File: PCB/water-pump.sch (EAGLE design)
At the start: 26 parts, among them U1 LDL1117S12R, U3 ATSAMD11C14A-SSUT

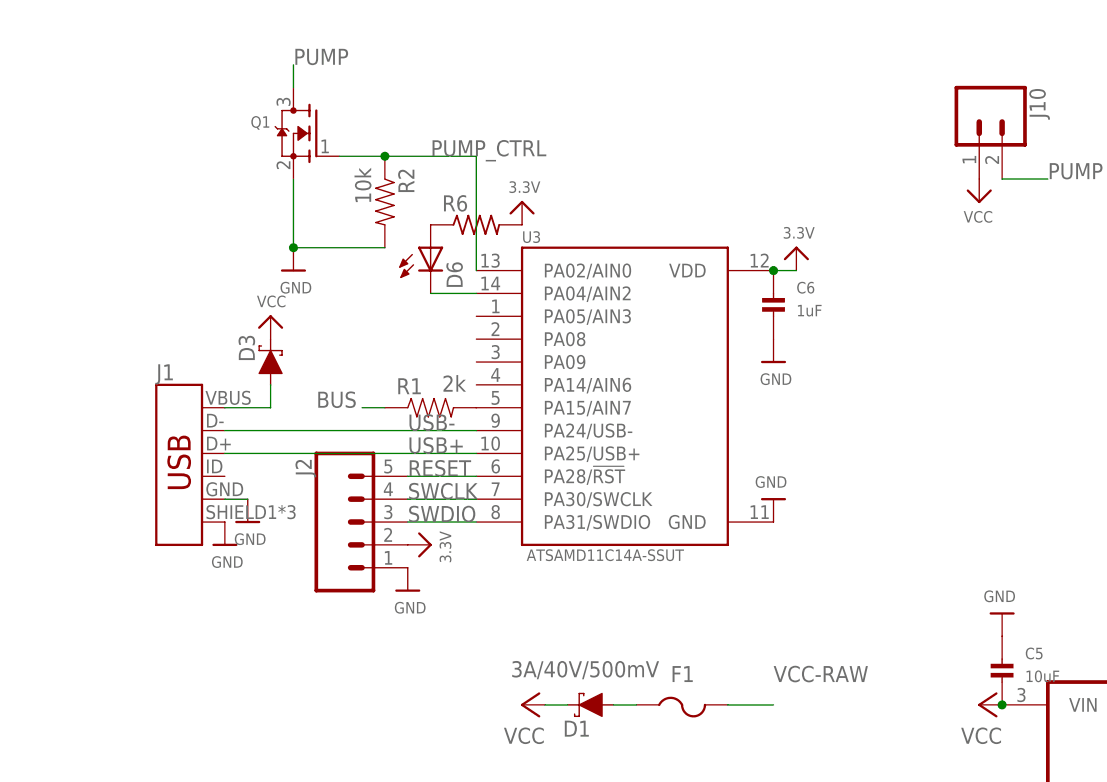
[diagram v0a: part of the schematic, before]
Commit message: added button to pcbs and did some fixing
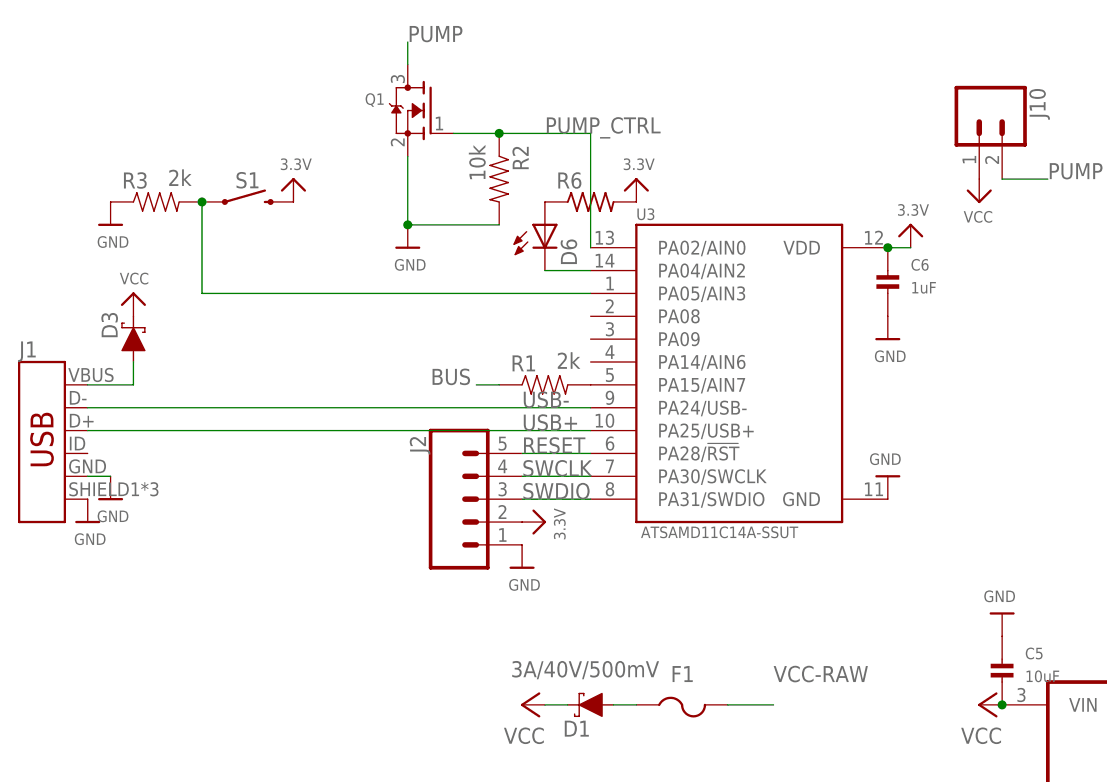
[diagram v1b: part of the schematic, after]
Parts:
- added R3: 2k, SparkFun-Resistors:RESISTOR1206
- added S1: MOMENTARY-SWITCH-SPST-SMD-6.0X3.5MM, SparkFun-Switches:MOMENTARY-SWITCH-SPST-SMD-6.0X3.5MM
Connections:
- new net N$4: R3.2, S1.1, U3.PA05/AIN3
- net 3.3V: now also S1.2
- net GND: now also R3.1
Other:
- moved on the sheet: C6, D3, D6, J1, J2, Q1, R1, R2, R6, U3

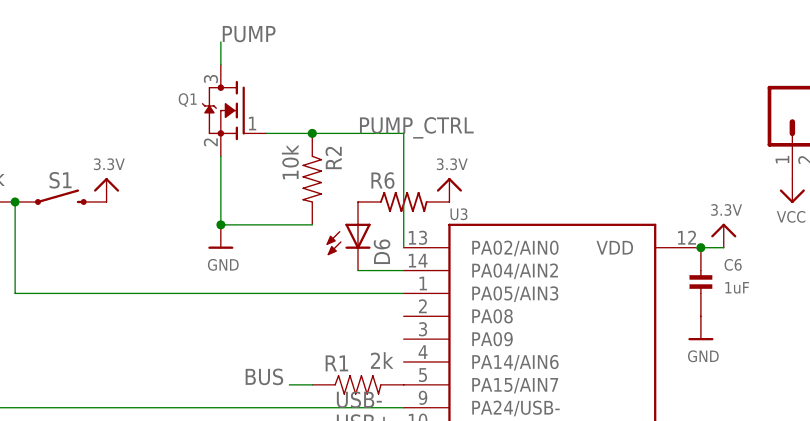
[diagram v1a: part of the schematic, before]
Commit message: added missing resistor before mosfet
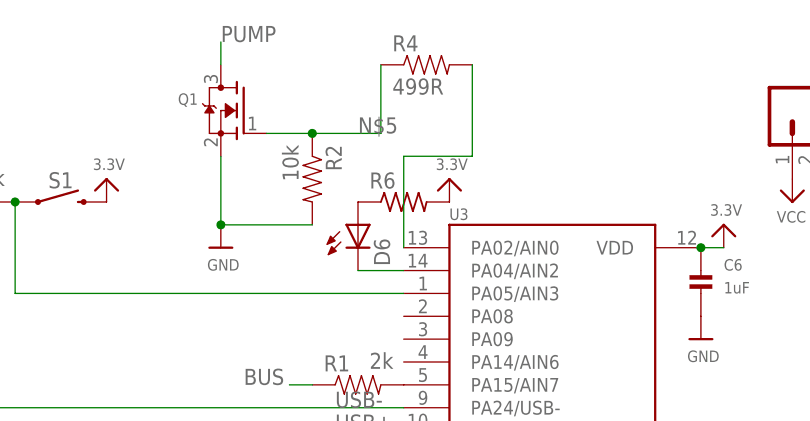
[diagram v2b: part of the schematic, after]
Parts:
- added R4: 499R, SparkFun-Resistors:RESISTOR1206
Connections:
- new net N$5: Q1.G, R2.1, R4.1
- net PUMP_CTRL: now also R4.2; no longer Q1.G, R2.1
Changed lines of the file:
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@@
 <?xml version="1.0" encoding="utf-8"?>
 <!DOCTYPE eagle SYSTEM "eagle.dtd">
-<eagle version="9.2.2">
+<eagle version="9.3.0">
 <drawing>
 <settings>
@@
 <part name="R3" library="SparkFun-Resistors" deviceset="RESISTOR" device="1206" value="2k"/>
 <part name="S1" library="SparkFun-Switches" deviceset="MOMENTARY-SWITCH-SPST" device="-SMD-6.0X3.5MM"/>
+<part name="R4" library="SparkFun-Resistors" deviceset="RESISTOR" device="1206" value="499R"/>
 </parts>
 <sheets>
@@
 <attribute name="NAME" x="-81.28" y="67.564" size="1.778" layer="95" font="vector" align="bottom-center"/>
 </instance>
+<instance part="R4" gate="G$1" x="-40.64" y="81.28" smashed="yes">
+<attribute name="NAME" x="-44.45" y="82.7786" size="1.778" layer="95"/>
+<attribute name="VALUE" x="-44.45" y="77.978" size="1.778" layer="96"/>
+</instance>
 </instances>
 <busses>
@@
 <net name="PUMP_CTRL" class="0">
 <segment>
-<pinref part="R2" gate="G$1" pin="1"/>
-<label x="-48.26" y="73.66" size="1.778" layer="95"/>
 <pinref part="U3" gate="G$1" pin="PA02/AIN0"/>
-<wire x1="-53.34" y1="73.66" x2="-43.18" y2="73.66" width="0.1524" layer="91"/>
-<wire x1="-43.18" y1="73.66" x2="-43.18" y2="60.96" width="0.1524" layer="91"/>
-<pinref part="Q1" gate="G$1" pin="G"/>
-<wire x1="-58.42" y1="73.66" x2="-53.34" y2="73.66" width="0.1524" layer="91"/>
-<junction x="-53.34" y="73.66"/>
+<wire x1="-43.18" y1="71.12" x2="-43.18" y2="60.96" width="0.1524" layer="91"/>
+<pinref part="R4" gate="G$1" pin="2"/>
+<wire x1="-43.18" y1="71.12" x2="-35.56" y2="71.12" width="0.1524" layer="91"/>
+<wire x1="-35.56" y1="71.12" x2="-35.56" y2="81.28" width="0.1524" layer="91"/>
 </segment>
 </net>
@@
 </segment>
 </net>
+<net name="N$5" class="0">
+<segment>
+<pinref part="R4" gate="G$1" pin="1"/>
+<wire x1="-45.72" y1="73.66" x2="-45.72" y2="81.28" width="0.1524" layer="91"/>
+<pinref part="R2" gate="G$1" pin="1"/>
+<wire x1="-53.34" y1="73.66" x2="-45.72" y2="73.66" width="0.1524" layer="91"/>
+<junction x="-53.34" y="73.66"/>
+<pinref part="Q1" gate="G$1" pin="G"/>
+<wire x1="-58.42" y1="73.66" x2="-53.34" y2="73.66" width="0.1524" layer="91"/>
+<label x="-48.26" y="73.66" size="1.778" layer="95"/>
+</segment>
+</net>

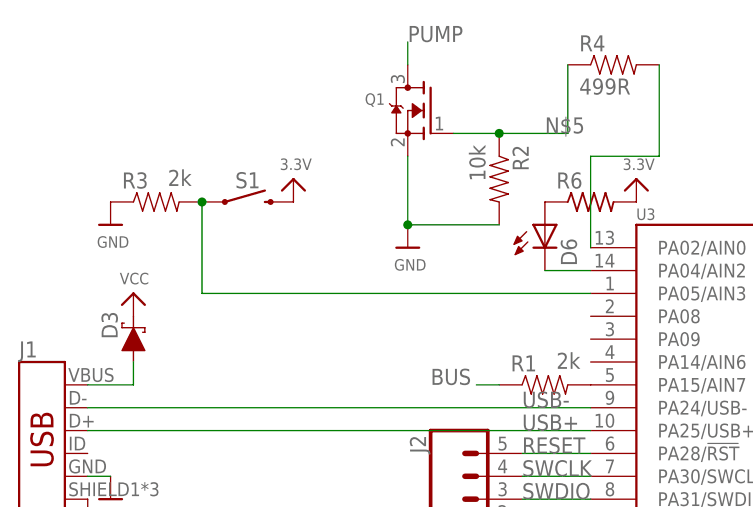
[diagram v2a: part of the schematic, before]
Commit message: removed buttons.. not needed
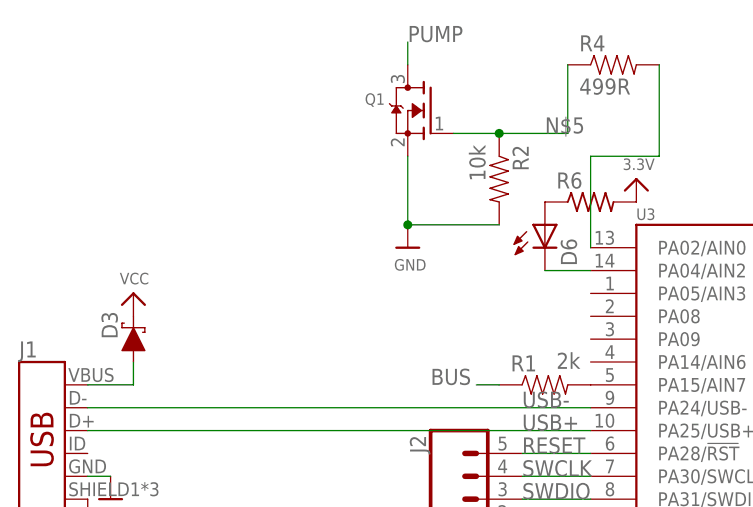
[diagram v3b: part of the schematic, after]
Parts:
- removed R3: 2k, SparkFun-Resistors:RESISTOR1206
- removed S1: MOMENTARY-SWITCH-SPST-SMD-6.0X3.5MM, SparkFun-Switches:MOMENTARY-SWITCH-SPST-SMD-6.0X3.5MM
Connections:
- removed net N$4: R3.2, S1.1, U3.PA05/AIN3
- net 3.3V: no longer S1.2
- net GND: no longer R3.1
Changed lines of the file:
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@@
 <part name="U$13" library="microbuilder" deviceset="3.3V" device=""/>
 <part name="P+7" library="supply1" library_urn="urn:adsk.eagle:library:371" deviceset="VCC" device=""/>
-<part name="U$14" library="microbuilder" deviceset="3.3V" device=""/>
-<part name="U$15" library="microbuilder" deviceset="GND" device=""/>
-<part name="R3" library="SparkFun-Resistors" deviceset="RESISTOR" device="1206" value="2k"/>
-<part name="S1" library="SparkFun-Switches" deviceset="MOMENTARY-SWITCH-SPST" device="-SMD-6.0X3.5MM"/>
 <part name="R4" library="SparkFun-Resistors" deviceset="RESISTOR" device="1206" value="499R"/>
 </parts>
@@
 <attribute name="VALUE" x="2.54" y="7.62" size="1.778" layer="96" rot="R180"/>
 </instance>
-<instance part="U$14" gate="G$1" x="-76.2" y="68.58" smashed="yes">
-<attribute name="VALUE" x="-77.724" y="69.596" size="1.27" layer="96"/>
-</instance>
-<instance part="U$15" gate="G$1" x="-96.52" y="63.5" smashed="yes">
-<attribute name="VALUE" x="-98.044" y="60.96" size="1.27" layer="96"/>
-</instance>
-<instance part="R3" gate="G$1" x="-91.44" y="66.04" smashed="yes">
-<attribute name="NAME" x="-95.25" y="67.5386" size="1.778" layer="95"/>
-<attribute name="VALUE" x="-90.17" y="67.818" size="1.778" layer="96"/>
-</instance>
-<instance part="S1" gate="G$1" x="-81.28" y="66.04" smashed="yes">
-<attribute name="NAME" x="-81.28" y="67.564" size="1.778" layer="95" font="vector" align="bottom-center"/>
-</instance>
 <instance part="R4" gate="G$1" x="-40.64" y="81.28" smashed="yes">
 <attribute name="NAME" x="-44.45" y="82.7786" size="1.778" layer="95"/>
@@
 <pinref part="U$8" gate="G$1" pin="GND"/>
 <wire x1="-99.06" y1="35.56" x2="-96.52" y2="35.56" width="0.1524" layer="91"/>
-</segment>
-<segment>
-<pinref part="U$15" gate="G$1" pin="GND"/>
-<pinref part="R3" gate="G$1" pin="1"/>
 </segment>
 </net>
@@
 <pinref part="U$11" gate="G$1" pin="3.3V"/>
 </segment>
-<segment>
-<pinref part="S1" gate="G$1" pin="2"/>
-<pinref part="U$14" gate="G$1" pin="3.3V"/>
-</segment>
-</net>
-<net name="N$4" class="0">
-<segment>
-<pinref part="R3" gate="G$1" pin="2"/>
-<pinref part="S1" gate="G$1" pin="1"/>
-<pinref part="U3" gate="G$1" pin="PA05/AIN3"/>
-<wire x1="-43.18" y1="55.88" x2="-86.36" y2="55.88" width="0.1524" layer="91"/>
-<wire x1="-86.36" y1="55.88" x2="-86.36" y2="66.04" width="0.1524" layer="91"/>
-<junction x="-86.36" y="66.04"/>
-</segment>
-</net>
+</net>
